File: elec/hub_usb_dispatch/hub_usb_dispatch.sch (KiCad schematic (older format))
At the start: 58 parts, among them IC1 TS2596CM550_RNG, J1 USB_B_Mini, J10 Conn_01x02, J11 Emergency Stop, J12 Switch Logic, J13 BAT_POWER Display, J14 BAT_LOGIC Display, J15 Conn_01x02, J16 Conn_01x02, J17 Conn_01x02, J2 USB_A_Stacked_Double, J3 Conn_01x02, J4 Conn_01x02, J5 USB_A, J6 USB_A_Stacked_Double, J7 USB_A_Stacked_Double, J8 Conn_01x02, J9 Conn_01x02, U1 MIC5504-3.3YM5, U2 USB2517, Y1 24M

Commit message: ESD protection on data lines
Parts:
- removed R5, R6: 100k, Resistor_SMD:R_0805_2012Metric, symbol Device:R
- added D1, D10, D11, D12, D13, D14, D15, D16, D2, D3, D4, D5, D6, D7, D8, D9: ESD9B3.3ST5G, villanut_lib:ESD9B3.3ST5G, symbol Device:D
- C3, C4: value 18pF -> 33pF
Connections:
- net 1_D+: now also D1.1 (K)
- net 1_D-: now also D2.1 (K)
- net 2_D+: now also D14.1 (K)
- net 2_D-: now also D10.1 (K)
- net 3_D+: now also D5.1 (K)
- net 3_D-: now also D7.1 (K)
- net 4_D+: now also D15.1 (K)
- net 4_D-: now also D11.1 (K)
- net 5_D+: now also D6.1 (K)
- net 5_D-: now also D8.1 (K)
- net 6_D+: now also D16.1 (K)
- net 6_D-: now also D12.1 (K)
- net 7_D+: now also D13.1 (K)
- net 7_D-: now also D9.1 (K)
- net D+: now also D4.1 (K)
- net D-: now also D3.1 (K)
- net GND: now also D1.2 (A), D10.2 (A), D11.2 (A), D12.2 (A), D13.2 (A), D14.2 (A), D15.2 (A), D16.2 (A), D2.2 (A), D3.2 (A), D4.2 (A), D5.2 (A), D6.2 (A), D7.2 (A), D8.2 (A), D9.2 (A)
- net at U2.44 (VBUS_DET): now also C5.1, J1.1 (VBUS)

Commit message: Fix schematic
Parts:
- added C24, C27, C28: 100nF, symbol Device:C
- added C25, C26, C29: 1uF, symbol Device:C
- added R10, R11, R12, R13, R5: 10k, symbol Device:R
- added R6: 100k, symbol Device:R
- D1, D10, D11, D12, D13, D14, D15, D16, D2, D3, D4, D5, D6, D7, D8, D9: value ESD9B3.3ST5G -> CG0603MLC-3.3LEA; footprint villanut_lib:ESD9B3.3ST5G -> (none)
- R1, R2: value 56k -> 100k; footprint Resistor_SMD:R_0805_2012Metric -> (none)
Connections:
- net +3V3: now also R1.2, C29.1, R10.1, R11.1, R12.1, R5.1; no longer U2.43 (RESET_N)
- net 1_D+: now also D3.1 (K); no longer D1.1 (K)
- net 1_D-: now also D6.1 (K); no longer D2.1 (K)
- net 3_D+: now also D4.1 (K); no longer D5.1 (K)
- net 5_D+: now also D5.1 (K); no longer D6.1 (K)
- net D+: now also D2.1 (K); no longer D4.1 (K)
- net D-: now also D1.1 (K); no longer D3.1 (K)
- net GND: now also C24.2, C25.2, C26.2, C27.2, C28.2, C29.2, R13.2, R6.1; no longer R1.2, R2.2, U2.40 (SDA/SMBDAFA/NON_REM1), U2.41 (SCL/SMBCLK/CFG_SEL0)
- net at U2.13 (CFG_SEL2): now also R5.2
- net at U2.25 (CRFILT): now also U2.62 (PLLFILT), C25.1, C26.1, C27.1, C28.1
- net at U2.42 (HS_IND/CFG_SEL1): now also R13.1; no longer R2.1
- net at C5.1, J1.1 (VBUS): now also R2.2; no longer U2.44 (VBUS_DET)
- net at U2.45 (SUSP_IND/LOCAL_PWR/NON_REM0): now also R12.2; no longer R1.1
- new net: R11.2, U2.40 (SDA/SMBDAFA/NON_REM1)
- new net: R10.2, U2.41 (SCL/SMBCLK/CFG_SEL0)
- new net RESET_N: C24.1, R1.1, U2.43 (RESET_N)
- new net VBUS_DET: R2.1, R6.2, U2.44 (VBUS_DET)
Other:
- moved on the sheet: C11, C13, C15, C19, C5, C6, C7, C8, C9, J1

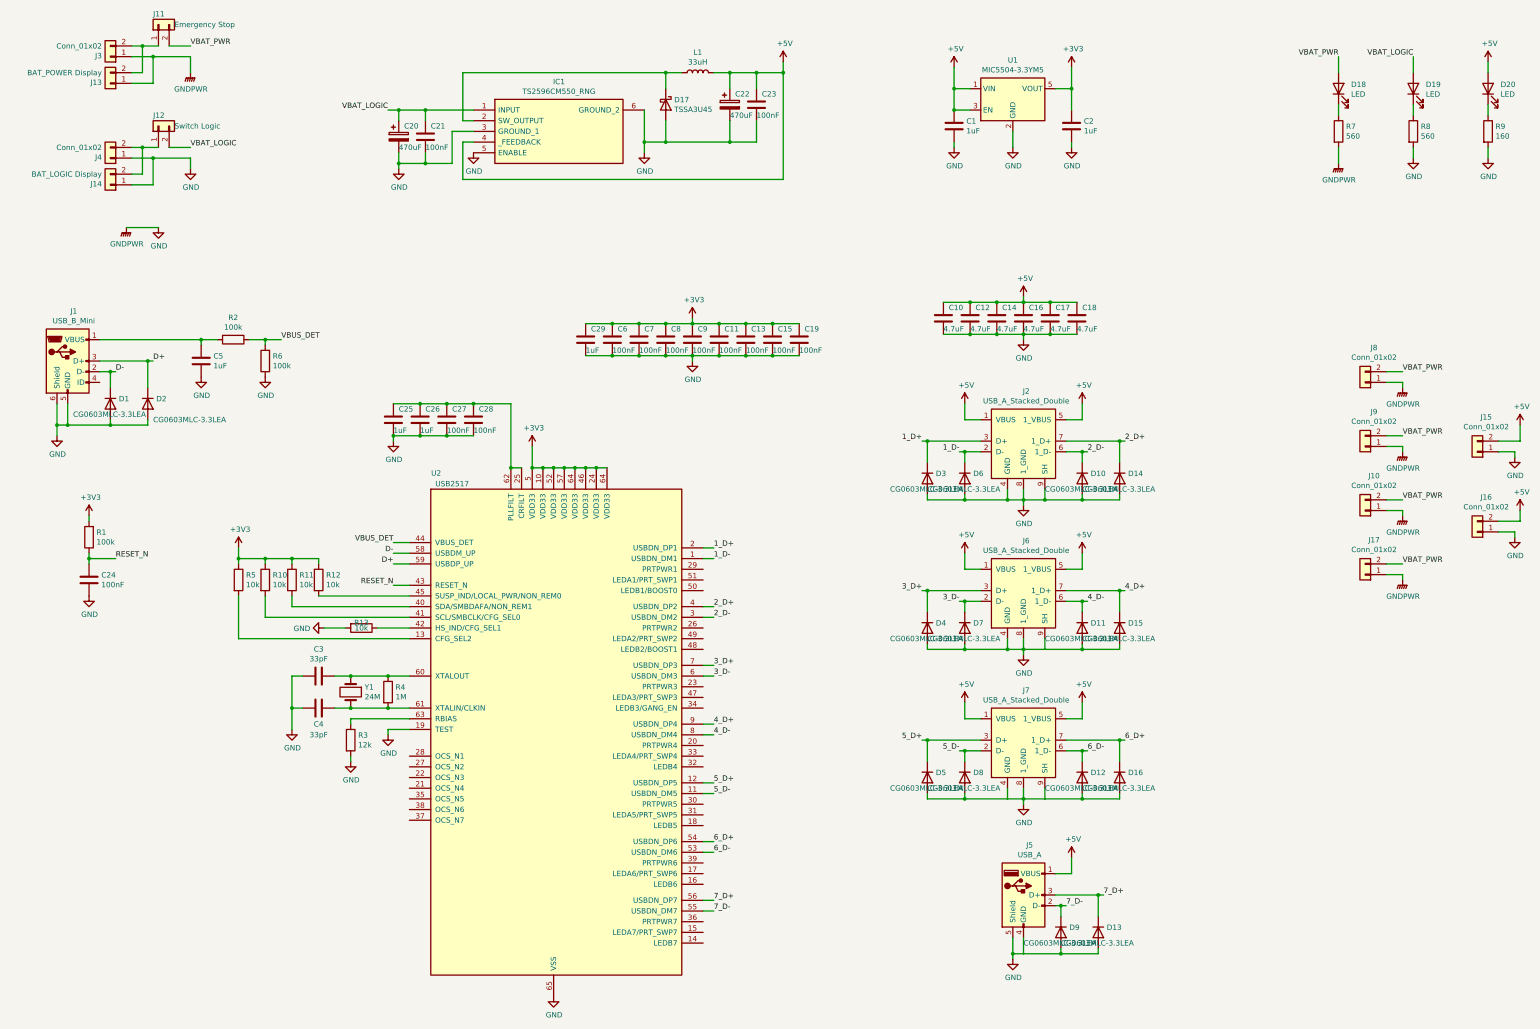
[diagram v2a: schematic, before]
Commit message: V2.0 : fix dumb mistakes (capacitors pin 25 and 62, lower capacitance ESD diodes, RESET_N R-C, CFG_SEL2 and VBUS_DET resistor divider)
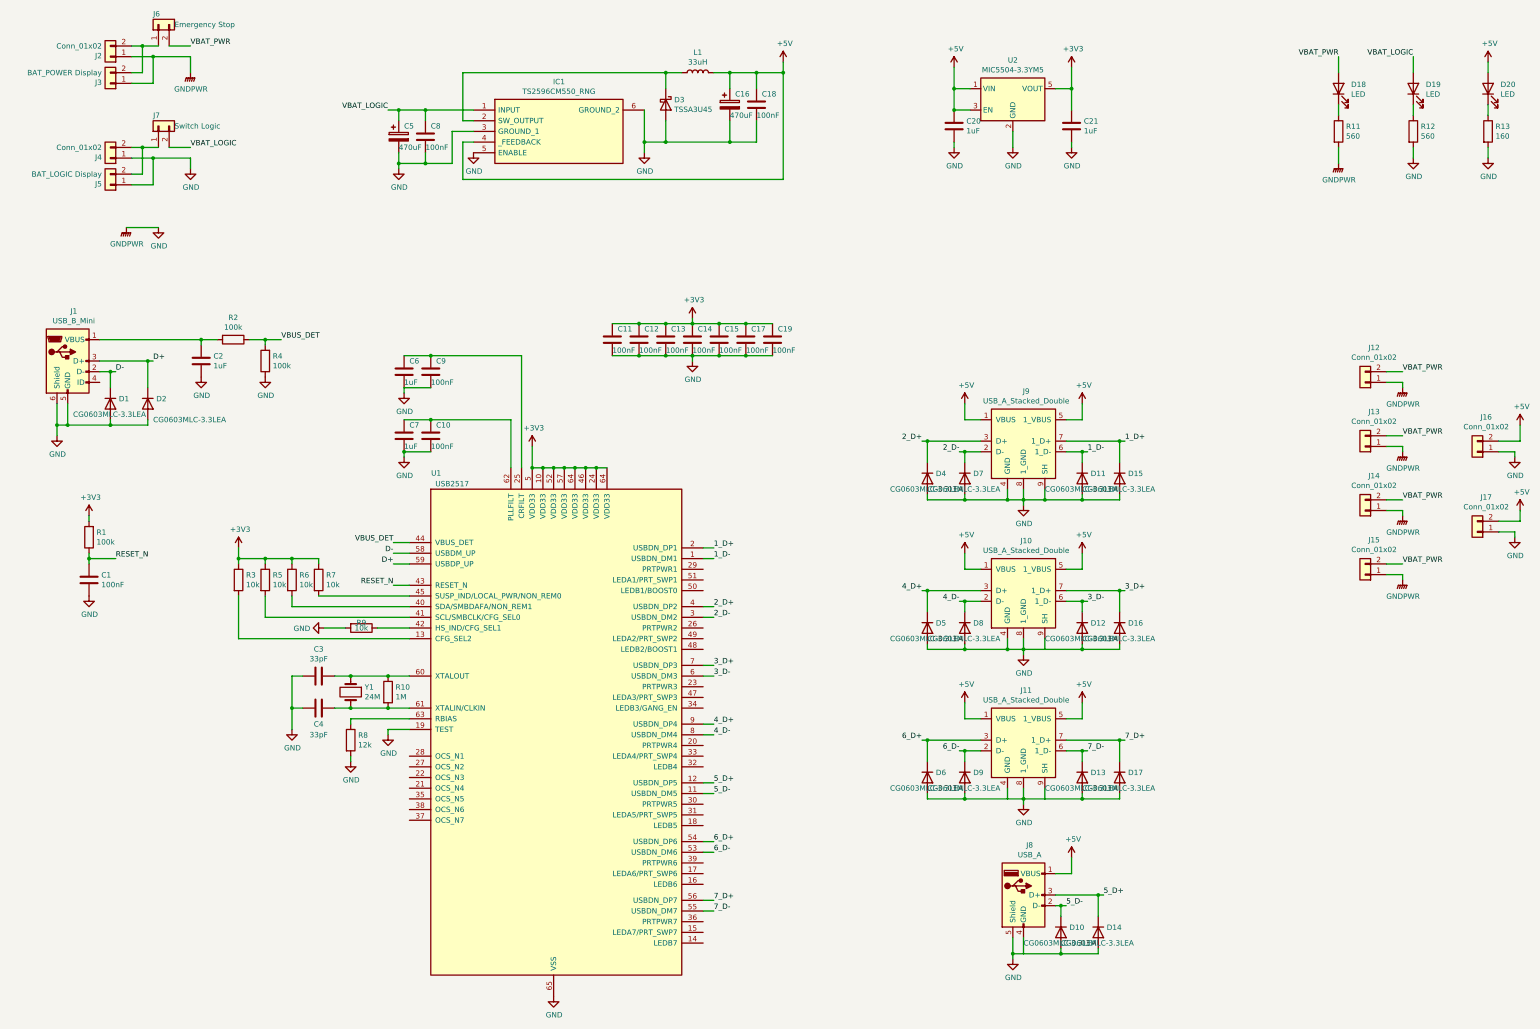
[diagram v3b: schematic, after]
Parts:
- removed C10, C12, C14, C16, C17, C18: 4.7uF, Capacitor_SMD:C_0805_2012Metric, symbol Device:C
- removed C19: 100nF, Capacitor_SMD:C_0805_2012Metric, symbol Device:C
- removed C29: 1uF, symbol Device:C
- C1: renamed from C24; footprint (none) -> Capacitor_SMD:C_0805_2012Metric
- C10: renamed from C27; footprint (none) -> Capacitor_SMD:C_0805_2012Metric
- C6: renamed from C26; footprint (none) -> Capacitor_SMD:C_0805_2012Metric
- C7: renamed from C25; footprint (none) -> Capacitor_SMD:C_0805_2012Metric
- C9: renamed from C28; footprint (none) -> Capacitor_SMD:C_0805_2012Metric
- D1, D2: footprint (none) -> Diode_SMD:D_0603_1608Metric
- D10: renamed from D9; footprint (none) -> Diode_SMD:D_0603_1608Metric
- D11: renamed from D10; footprint (none) -> Diode_SMD:D_0603_1608Metric
- D12: renamed from D11; footprint (none) -> Diode_SMD:D_0603_1608Metric
- D13: renamed from D12; footprint (none) -> Diode_SMD:D_0603_1608Metric
- D14: renamed from D13; footprint (none) -> Diode_SMD:D_0603_1608Metric
- D15: renamed from D14; footprint (none) -> Diode_SMD:D_0603_1608Metric
- D16: renamed from D15; footprint (none) -> Diode_SMD:D_0603_1608Metric
- D17: renamed from D16; footprint (none) -> Diode_SMD:D_0603_1608Metric
- D4: renamed from D3; footprint (none) -> Diode_SMD:D_0603_1608Metric
- D5: renamed from D4; footprint (none) -> Diode_SMD:D_0603_1608Metric
- D6: renamed from D5; footprint (none) -> Diode_SMD:D_0603_1608Metric
- D7: renamed from D6; footprint (none) -> Diode_SMD:D_0603_1608Metric
- D8: renamed from D7; footprint (none) -> Diode_SMD:D_0603_1608Metric
- D9: renamed from D8; footprint (none) -> Diode_SMD:D_0603_1608Metric
- R1, R2: footprint (none) -> Resistor_SMD:R_0805_2012Metric
- R3: renamed from R5; footprint (none) -> Resistor_SMD:R_0805_2012Metric
- R4: renamed from R6; footprint (none) -> Resistor_SMD:R_0805_2012Metric
- R5: renamed from R10; footprint (none) -> Resistor_SMD:R_0805_2012Metric
- R6: renamed from R11; footprint (none) -> Resistor_SMD:R_0805_2012Metric
- R7: renamed from R12; footprint (none) -> Resistor_SMD:R_0805_2012Metric
- R9: renamed from R13; footprint (none) -> Resistor_SMD:R_0805_2012Metric
- renumbered C6 to C11, C7 to C12, C8 to C13, C9 to C14, C11 to C15, C22 to C16, C13 to C17, C23 to C18, C15 to C19, C5 to C2, C1 to C20, C2 to C21, C20 to C5, C21 to C8, D17 to D3, J6 to J10, J7 to J11, J8 to J12, J9 to J13, J10 to J14, J17 to J15, J15 to J16, J16 to J17, J3 to J2, J13 to J3, J14 to J5, J11 to J6, J12 to J7, J5 to J8, J2 to J9, R4 to R10, R7 to R11, R8 to R12, R9 to R13, R3 to R8, U2 to U1, U1 to U2
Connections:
- net 1_D+: now also D15.1 (K), J9.7 (1_D+); no longer D4.1 (K), J9.3 (D+)
- net 1_D-: now also D11.1 (K), J9.6 (1_D-); no longer D7.1 (K), J9.2 (D-)
- net 2_D+: now also D4.1 (K), J9.3 (D+); no longer D15.1 (K), J9.7 (1_D+)
- net 2_D-: now also D7.1 (K), J9.2 (D-); no longer D11.1 (K), J9.6 (1_D-)
- net 3_D+: now also D16.1 (K), J10.7 (1_D+); no longer D5.1 (K), J10.3 (D+)
- net 3_D-: now also D12.1 (K), J10.6 (1_D-); no longer D8.1 (K), J10.2 (D-)
- net 4_D+: now also D5.1 (K), J10.3 (D+); no longer D16.1 (K), J10.7 (1_D+)
- net 4_D-: now also D8.1 (K), J10.2 (D-); no longer D12.1 (K), J10.6 (1_D-)
- net 5_D+: now also D14.1 (K), J8.3 (D+); no longer D6.1 (K), J11.3 (D+)
- net 5_D-: now also D10.1 (K), J8.2 (D-); no longer D9.1 (K), J11.2 (D-)
- net 6_D+: now also D6.1 (K), J11.3 (D+); no longer D17.1 (K), J11.7 (1_D+)
- net 6_D-: now also D9.1 (K), J11.2 (D-); no longer D13.1 (K), J11.6 (1_D-)
- net 7_D+: now also D17.1 (K), J11.7 (1_D+); no longer D14.1 (K), J8.3 (D+)
- net 7_D-: now also D13.1 (K), J11.6 (1_D-); no longer D10.1 (K), J8.2 (D-)
- net at C6.1, C9.1, U1.25 (CRFILT): no longer C10.1, C7.1, U1.62 (PLLFILT)
- new net: C10.1, C7.1, U1.62 (PLLFILT)
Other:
- moved on the sheet: C10, C6, C7, C9
